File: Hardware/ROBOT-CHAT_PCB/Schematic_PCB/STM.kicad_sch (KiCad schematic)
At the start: 30 parts, among them J1 Conn_01x04, J2 Conn_02x07_Odd_Even, J3 Conn_01x02, J4 Conn_01x02, SW1 SW_Push_Dual, U1 STM32WB55CEUx, Y1 32.768kHz, Y2 32MHz

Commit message: current schematic
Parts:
- removed J2: Conn_02x07_Odd_Even, symbol Connector_Generic:Conn_02x07_Odd_Even
- added J201: Conn_ST_STDC14, Connector_PinHeader_1.27mm:PinHeader_2x07_P1.27mm_Vertical_SMD, symbol Connector:Conn_ST_STDC14
- C10, C11, C12, C13, C15, C16, C3, C4, C5, C6, C7, C8, C9: footprint (none) -> Capacitor_SMD:C_0603_1608Metric
- C14, C17, C18: footprint (none) -> Capacitor_SMD:C_0402_1005Metric
- D1: footprint (none) -> LED_SMD:LED_0603_1608Metric
- J1: footprint (none) -> Connector_JST:JST_XH_B4B-XH-AM_1x04_P2.50mm_Vertical
- J3, J4: footprint (none) -> Connector_JST:JST_PH_B2B-PH-K_1x02_P2.00mm_Vertical
- L1, L2: footprint (none) -> Inductor_SMD:L_0603_1608Metric
- R4, R5, R6: footprint (none) -> Resistor_SMD:R_0603_1608Metric
- SW1: footprint Button_Switch_SMD2:SW_Push_1P1T_NO_6x6mm_H9.5mm -> SW_Push_1P1T_NO_6x6mm_H9.5mm:SW_Push_1P1T_NO_6x6mm_H9.5mm
- Y2: footprint ABS07AIG_32_768KHZ_7_T:XTAL320X150X90 -> XRCGB32M000F2P01R0:XRCGB32M000F2P01R0
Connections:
- net +3.3V: now also J201.3 (VCC)
- net GND: now also J201.11 (GNDDetect), J201.5 (GND), J201.7 (GND)
- net NRST: now also J201.12 (~{RST})
- net SWCLK: now also J201.6 (JCLK/SWCLK)
- net SWDIO: now also J201.4 (JTMS/SWDIO)
- net SWO: now also J201.8 (JTDO/SWO)
- net VCP_RX: now also J201.13 (VCP_RX)
- net VCP_TX: now also J201.14 (VCP_TX)
- net EN3.3: no longer names the net of U1.19 (PB2)
- net EN5: no longer names the net of U1.45 (PB5)

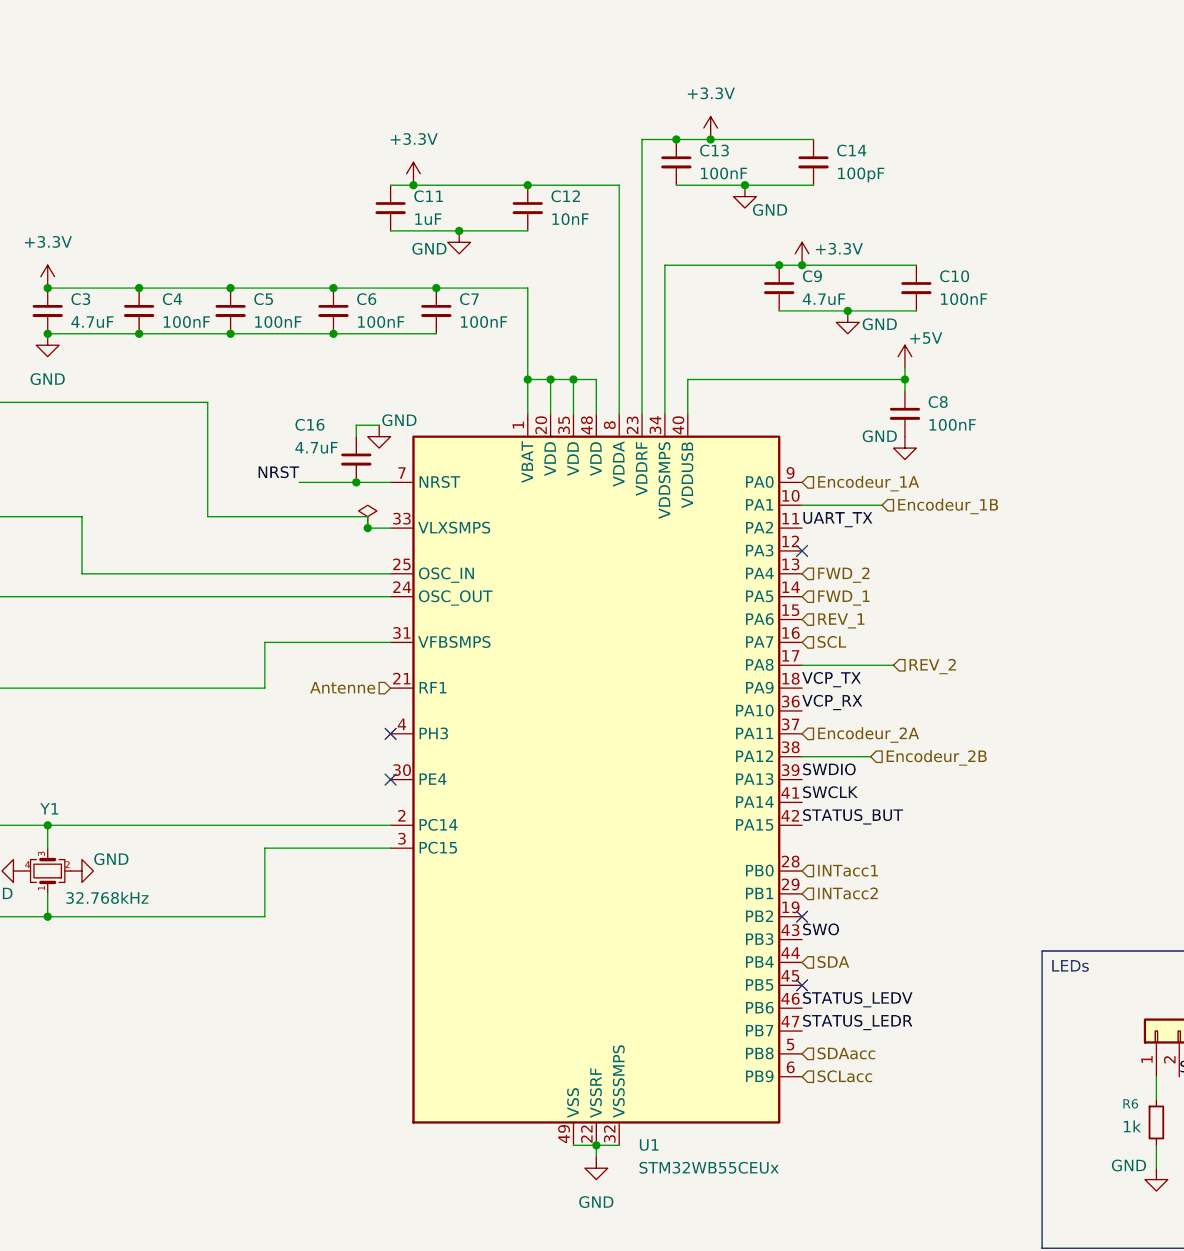
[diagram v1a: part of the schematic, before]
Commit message: Rerouting avec Mr Fiack
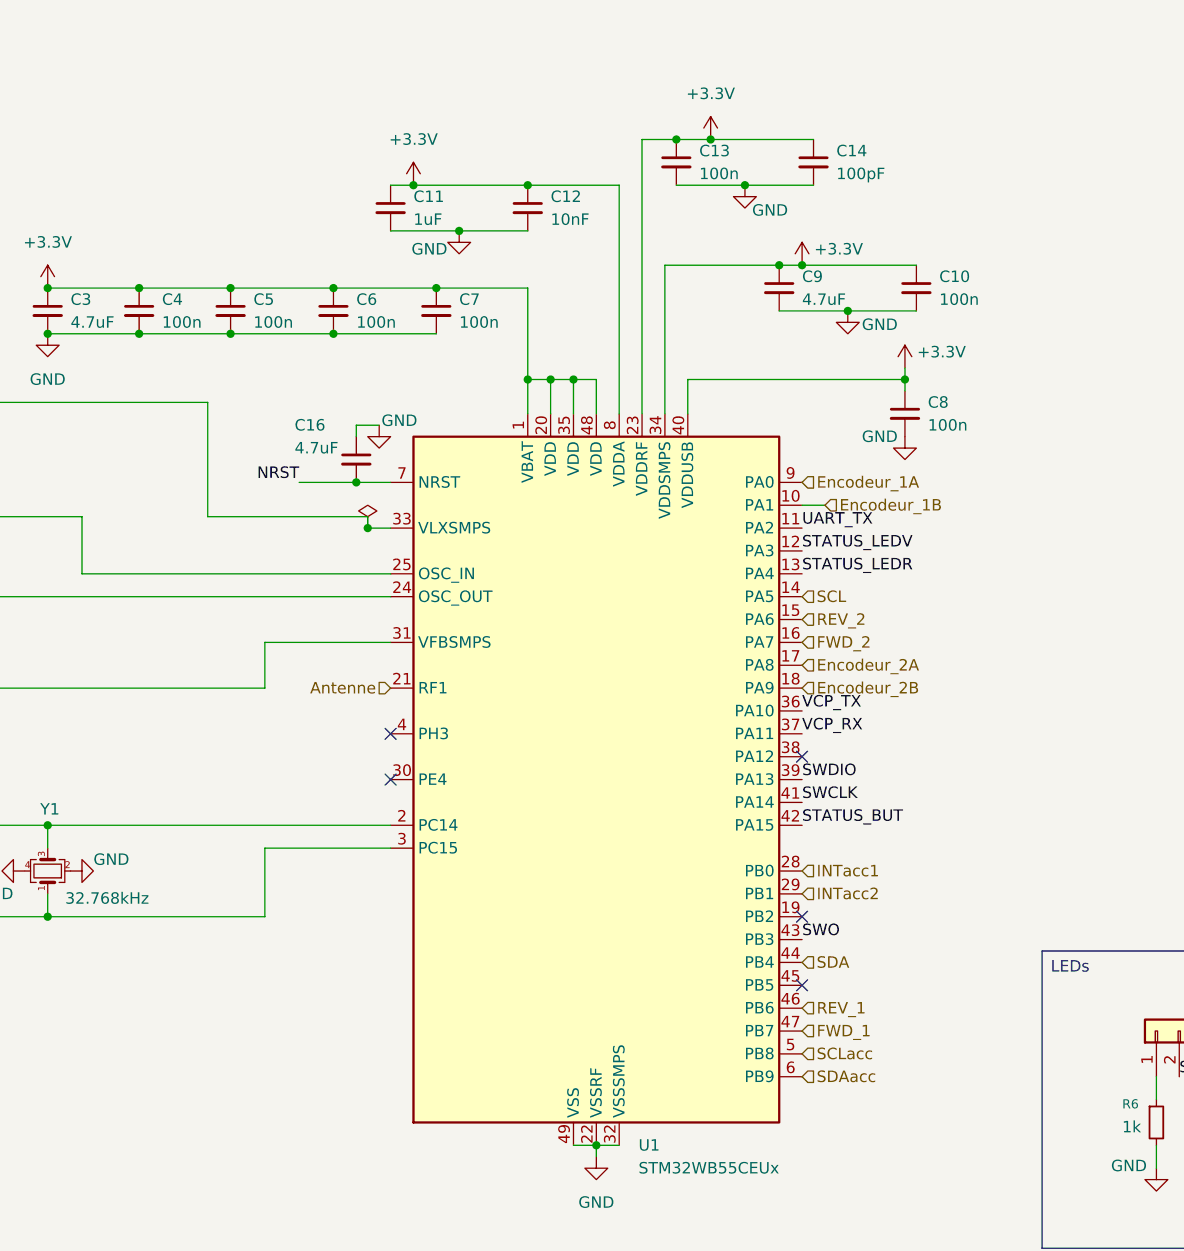
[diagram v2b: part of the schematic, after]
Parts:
- C10, C13, C4, C5, C6, C7, C8: value 100nF -> 100n; footprint Capacitor_SMD:C_0603_1608Metric -> Capacitor_SMD:C_0402_1005Metric
- C12: footprint Capacitor_SMD:C_0603_1608Metric -> Capacitor_SMD:C_0402_1005Metric
- R4, R5, R6: footprint Resistor_SMD:R_0603_1608Metric -> Resistor_SMD:R_0402_1005Metric
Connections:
- net +3.3V: now also C8.1, U1.40 (VDDUSB)
- net +5V: no longer C8.1, U1.40 (VDDUSB)
- net Encodeur_2A: now also U1.17 (PA8); no longer U1.37 (PA11)
- net Encodeur_2B: now also U1.18 (PA9); no longer U1.38 (PA12)
- net FWD_1: now also U1.47 (PB7); no longer U1.14 (PA5)
- net FWD_2: now also U1.16 (PA7); no longer U1.13 (PA4)
- net REV_1: now also U1.46 (PB6); no longer U1.15 (PA6)
- net REV_2: now also U1.15 (PA6); no longer U1.17 (PA8)
- net SCL: now also U1.14 (PA5); no longer U1.16 (PA7)
- net SCLacc: now also U1.5 (PB8); no longer U1.6 (PB9)
- net SDAacc: now also U1.6 (PB9); no longer U1.5 (PB8)
- net STATUS_LEDR: now also U1.13 (PA4); no longer U1.47 (PB7)
- net STATUS_LEDV: now also U1.12 (PA3); no longer U1.46 (PB6)
- net VCP_RX: now also U1.37 (PA11); no longer U1.36 (PA10)
- net VCP_TX: now also U1.36 (PA10); no longer U1.18 (PA9)
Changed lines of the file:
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@@
 	)
 	(no_connect
-		(at 177.8 82.55)
+		(at 177.8 105.41)
 	)
 	(no_connect
@@
 	(wire
 		(pts
-			(xy 185.42 105.41) (xy 177.8 105.41)
-		)
-		(stroke
-			(width 0)
-			(type default)
-		)
-	)
-	(wire
-		(pts
 			(xy 189.23 63.5) (xy 189.23 64.77)
 		)
@@
 	(wire
 		(pts
-			(xy 186.69 77.47) (xy 177.8 77.47)
-		)
-		(stroke
-			(width 0)
-			(type default)
-		)
-	)
-	(wire
-		(pts
-			(xy 187.96 95.25) (xy 177.8 95.25)
+			(xy 180.34 77.47) (xy 177.8 77.47)
 		)
 		(stroke
@@
 	)
 	(label "VCP_RX"
-		(at 177.8 100.33 0)
+		(at 177.8 102.87 0)
 		(effects
 			(font
@@
 	)
 	(label "VCP_TX"
-		(at 177.8 97.79 0)
+		(at 177.8 100.33 0)
 		(effects
 			(font
@@
 	)
 	(label "STATUS_LEDR"
-		(at 177.8 135.89 0)
+		(at 177.8 85.09 0)
 		(effects
 			(font
@@
 	)
 	(label "STATUS_LEDV"
-		(at 177.8 133.35 0)
+		(at 177.8 82.55 0)
 		(effects
 			(font
@@
 	(hierarchical_label "FWD_2"
 		(shape input)
-		(at 177.8 85.09 0)
+		(at 177.8 92.71 0)
 		(effects
 			(font
@@
 	(hierarchical_label "REV_1"
 		(shape input)
-		(at 177.8 90.17 0)
+		(at 177.8 133.35 0)
 		(effects
 			(font
@@
 	(hierarchical_label "Encodeur_2B"
 		(shape input)
-		(at 185.42 105.41 0)
+		(at 177.8 97.79 0)
 		(effects
 			(font
@@
 	(hierarchical_label "FWD_1"
 		(shape input)
-		(at 177.8 87.63 0)
+		(at 177.8 135.89 0)
 		(effects
 			(font
@@
 	(hierarchical_label "SDAacc"
 		(shape input)
-		(at 177.8 138.43 0)
+		(at 177.8 140.97 0)
 		(effects
 			(font
@@
 	(hierarchical_label "Encodeur_2A"
 		(shape input)
-		(at 177.8 102.87 0)
+		(at 177.8 95.25 0)
 		(effects
 			(font
@@
 	(hierarchical_label "SCLacc"
 		(shape input)
-		(at 177.8 140.97 0)
+		(at 177.8 138.43 0)
 		(effects
 			(font
@@
 	(hierarchical_label "REV_2"
 		(shape input)
-		(at 187.96 95.25 0)
+		(at 177.8 90.17 0)
 		(effects
 			(font
@@
 	(hierarchical_label "Encodeur_1B"
 		(shape input)
-		(at 186.69 77.47 0)
+		(at 180.34 77.47 0)
 		(effects
 			(font
@@
 	(hierarchical_label "SCL"
 		(shape input)
-		(at 177.8 92.71 0)
+		(at 177.8 87.63 0)
 		(effects
 			(font
@@
 			)
 		)
-		(property "Value" "100nF"
+		(property "Value" "100n"
 			(at 191.77 68.5862 0)
 			(effects
@@
 			)
 		)
-		(property "Footprint" "Capacitor_SMD:C_0603_1608Metric"
+		(property "Footprint" "Capacitor_SMD:C_0402_1005Metric"
 			(at 189.23 67.31 0)
 			(effects
@@
 			)
 		)
-		(property "Footprint" "Resistor_SMD:R_0603_1608Metric"
+		(property "Footprint" "Resistor_SMD:R_0402_1005Metric"
 			(at 217.17 146.05 0)
 			(effects
@@
 			)
 		)
-		(property "Footprint" "Capacitor_SMD:C_0603_1608Metric"
+		(property "Footprint" "Capacitor_SMD:C_0402_1005Metric"
 			(at 147.32 44.45 0)
 			(effects
@@
 			)
 		)
-		(property "Value" "100nF"
+		(property "Value" "100n"
 			(at 139.7 57.1562 0)
 			(effects
@@
 			)
 		)
-		(property "Footprint" "Capacitor_SMD:C_0603_1608Metric"
+		(property "Footprint" "Capacitor_SMD:C_0402_1005Metric"
 			(at 137.16 55.88 0)
 			(effects
@@
 			)
 		)
-		(property "Footprint" "Resistor_SMD:R_0603_1608Metric"
+		(property "Footprint" "Resistor_SMD:R_0402_1005Metric"
 			(at 242.57 146.05 0)
 			(effects
@@
 	)
 	(symbol
+		(lib_id "power:+3.3V")
+		(at 189.23 62.23 0)
+		(unit 1)
+		(exclude_from_sim no)
+		(in_bom yes)
+		(on_board yes)
+		(dnp no)
+		(property "Reference" "#PWR0201"
+			(at 189.23 66.04 0)
+			(effects
+				(font
+					(size 1.27 1.27)
+				)
+				(hide yes)
+			)
+		)
+		(property "Value" "+3.3V"
+			(at 193.294 60.452 0)
+			(effects
+				(font
+					(size 1.27 1.27)
+				)
+			)
+		)
+		(property "Footprint" ""
+			(at 189.23 62.23 0)
+			(effects
+				(font
+					(size 1.27 1.27)
+				)
+				(hide yes)
+			)
+		)
+		(property "Datasheet" ""
+			(at 189.23 62.23 0)
+			(effects
+				(font
+					(size 1.27 1.27)
+				)
+				(hide yes)
+			)
+		)
+		(property "Description" "Power symbol creates a global label with name \"+3.3V\""
+			(at 189.23 62.23 0)
+			(effects
+				(font
+					(size 1.27 1.27)
+				)
+				(hide yes)
+			)
+		)
+		(pin "1"
+		)
+		(instances
+			(project "PCB_robot_chat"
+				(path "/3534a4da-1897-4a3c-809d-843e7f41fadb/6dd21f76-e181-4380-95ef-cbdd4cbc38f9"
+					(reference "#PWR0201")
+					(unit 1)
+				)
+			)
+		)
+	)
+	(symbol
 		(lib_id "Device:C_Small")
 		(at 163.83 39.37 0)
@@
 			)
 		)
-		(property "Value" "100nF"
+		(property "Value" "100n"
 			(at 166.37 40.6462 0)
 			(effects
@@
 			)
 		)
-		(property "Footprint" "Capacitor_SMD:C_0603_1608Metric"
+		(property "Footprint" "Capacitor_SMD:C_0402_1005Metric"
 			(at 163.83 39.37 0)
 			(effects
@@
 			)
 		)
-		(property "Value" "100nF"
+		(property "Value" "100n"
 			(at 106.68 57.1562 0)
 			(effects
@@
 			)
 		)
-		(property "Footprint" "Capacitor_SMD:C_0603_1608Metric"
+		(property "Footprint" "Capacitor_SMD:C_0402_1005Metric"
 			(at 104.14 55.88 0)
 			(effects
@@
 			)
 		)
-		(property "Value" "100nF"
+		(property "Value" "100n"
 			(at 128.27 57.1562 0)
 			(effects
@@
 			)
 		)
-		(property "Footprint" "Capacitor_SMD:C_0603_1608Metric"
+		(property "Footprint" "Capacitor_SMD:C_0402_1005Metric"
 			(at 125.73 55.88 0)
 			(effects
@@
 			)
 		)
-		(property "Value" "100nF"
+		(property "Value" "100n"
 			(at 116.84 57.1562 0)
 			(effects
@@
 			)
 		)
-		(property "Footprint" "Capacitor_SMD:C_0603_1608Metric"
+		(property "Footprint" "Capacitor_SMD:C_0402_1005Metric"
 			(at 114.3 55.88 0)
 			(effects
@@
 	)
 	(symbol
-		(lib_id "power:+5V")
-		(at 189.23 62.23 0)
-		(unit 1)
-		(exclude_from_sim no)
-		(in_bom yes)
-		(on_board yes)
-		(dnp no)
-		(property "Reference" "#PWR015"
-			(at 189.23 66.04 0)
-			(effects
-				(font
-					(size 1.27 1.27)
-				)
-				(hide yes)
-			)
-		)
-		(property "Value" "+5V"
-			(at 191.516 58.928 0)
-			(effects
-				(font
-					(size 1.27 1.27)
-				)
-			)
-		)
-		(property "Footprint" ""
-			(at 189.23 62.23 0)
-			(effects
-				(font
-					(size 1.27 1.27)
-				)
-				(hide yes)
-			)
-		)
-		(property "Datasheet" ""
-			(at 189.23 62.23 0)
-			(effects
-				(font
-					(size 1.27 1.27)
-				)
-				(hide yes)
-			)
-		)
-		(property "Description" "Power symbol creates a global label with name \"+5V\""
-			(at 189.23 62.23 0)
-			(effects
-				(font
-					(size 1.27 1.27)
-				)
-				(hide yes)
-			)
-		)
-		(pin "1"
-		)
-		(instances
-			(project "PCB_robot_chat"
-				(path "/3534a4da-1897-4a3c-809d-843e7f41fadb/6dd21f76-e181-4380-95ef-cbdd4cbc38f9"
-					(reference "#PWR015")
-					(unit 1)
-				)
-			)
-		)
-	)
-	(symbol
 		(lib_id "Device:C_Small")
 		(at 190.5 53.34 0)
@@
 			)
 		)
-		(property "Value" "100nF"
+		(property "Value" "100n"
 			(at 193.04 54.6162 0)
 			(effects
@@
 			)
 		)
-		(property "Footprint" "Capacitor_SMD:C_0603_1608Metric"
+		(property "Footprint" "Capacitor_SMD:C_0402_1005Metric"
 			(at 190.5 53.34 0)
 			(effects
@@
 			)
 		)
-		(property "Footprint" "Resistor_SMD:R_0603_1608Metric"
+		(property "Footprint" "Resistor_SMD:R_0402_1005Metric"
 			(at 265.43 148.59 0)
 			(effects

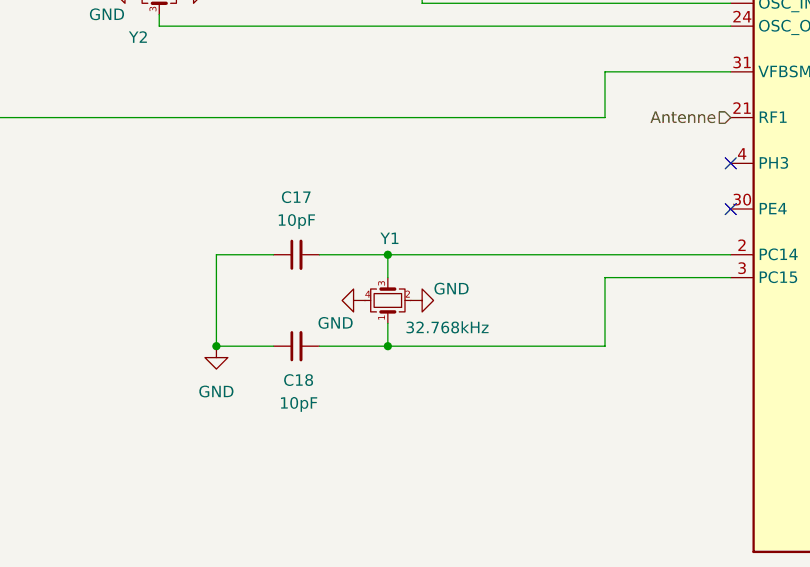
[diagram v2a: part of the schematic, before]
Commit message: Routage terminée, début serigraphie
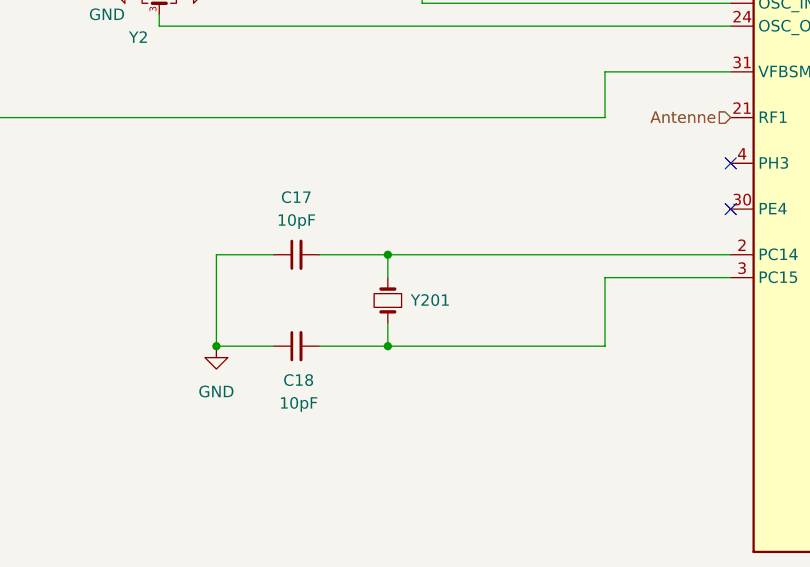
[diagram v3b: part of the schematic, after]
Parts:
- removed Y1: 32.768kHz, XRCGB32M000F2P01R0:XRCGB32M000F2P01R0, symbol Device:Crystal_GND24_Small
- added Y201: Crystal_Small, ABS07AIG-32.768KHZ-6-D-T:ABS07AIG-32.768KHZ-6-D-T, symbol Device:Crystal_Small
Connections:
- net at C18.2, U1.3 (PC15): now also Y201.1
- net at C17.2, U1.2 (PC14): now also Y201.2
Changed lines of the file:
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@@
+	)
+	(symbol
+		(lib_id "Device:Crystal_Small")
+		(at 93.98 118.11 90)
+		(unit 1)
+		(exclude_from_sim no)
+		(in_bom yes)
+		(on_board yes)
+		(dnp no)
+		(fields_autoplaced yes)
+		(property "Reference" "Y201"
+			(at 96.52 118.1099 90)
+			(effects
+				(font
+					(size 1.27 1.27)
+				)
+				(justify right)
+			)
+		)
+		(property "Value" "Crystal_Small"
+			(at 96.52 119.3799 90)
+			(effects
+				(font
+					(size 1.27 1.27)
+				)
+				(justify right)
+				(hide yes)
+			)
+		)
+		(property "Footprint" "ABS07AIG-32.768KHZ-6-D-T:ABS07AIG-32.768KHZ-6-D-T"
+			(at 93.98 118.11 0)
+			(effects
+				(font
+					(size 1.27 1.27)
+				)
+				(hide yes)
+			)
+		)
+		(property "Datasheet" "~"
+			(at 93.98 118.11 0)
+			(effects
+				(font
+					(size 1.27 1.27)
+				)
+				(hide yes)
+			)
+		)
+		(property "Description" "Two pin crystal, small symbol"
+			(at 93.98 118.11 0)
+			(effects
+				(font
+					(size 1.27 1.27)
+				)
+				(hide yes)
+			)
+		)
+		(pin "2"
+		)
+		(pin "1"
+		)
+		(instances
+			(project ""
+				(path "/3534a4da-1897-4a3c-809d-843e7f41fadb/6dd21f76-e181-4380-95ef-cbdd4cbc38f9"
+					(reference "Y201")
+					(unit 1)
+				)
+			)
+		)
 	)
 	(symbol
@@
 	)
 	(symbol
-		(lib_id "Device:Crystal_GND24_Small")
-		(at 93.98 118.11 90)
-		(unit 1)
-		(exclude_from_sim no)
-		(in_bom yes)
-		(on_board yes)
-		(dnp no)
-		(property "Reference" "Y1"
-			(at 94.234 111.252 90)
-			(effects
-				(font
-					(size 1.27 1.27)
-				)
-			)
-		)
-		(property "Value" "32.768kHz"
-			(at 100.584 121.158 90)
-			(effects
-				(font
-					(size 1.27 1.27)
-				)
-			)
-		)
-		(property "Footprint" "XRCGB32M000F2P01R0:XRCGB32M000F2P01R0"
-			(at 93.98 118.11 0)
-			(effects
-				(font
-					(size 1.27 1.27)
-				)
-				(hide yes)
-			)
-		)
-		(property "Datasheet" "~"
-			(at 93.98 118.11 0)
-			(effects
-				(font
-					(size 1.27 1.27)
-				)
-				(hide yes)
-			)
-		)
-		(property "Description" "Four pin crystal, GND on pins 2 and 4, small symbol"
-			(at 93.98 118.11 0)
-			(effects
-				(font
-					(size 1.27 1.27)
-				)
-				(hide yes)
-			)
-		)
-		(pin "1"
-		)
-		(pin "2"
-		)
-		(pin "4"
-		)
-		(pin "3"
-		)
-		(instances
-			(project "PCB_robot_chat"
-				(path "/3534a4da-1897-4a3c-809d-843e7f41fadb/6dd21f76-e181-4380-95ef-cbdd4cbc38f9"
-					(reference "Y1")
-					(unit 1)
-				)
-			)
-		)
-	)
-	(symbol
 		(lib_id "power:GND")
 		(at 189.23 69.85 0)
@@
 	(symbol
 		(lib_id "power:GND")
-		(at 96.52 118.11 90)
-		(unit 1)
-		(exclude_from_sim no)
-		(in_bom yes)
-		(on_board yes)
-		(dnp no)
-		(property "Reference" "#PWR021"
-			(at 102.87 118.11 0)
-			(effects
-				(font
-					(size 1.27 1.27)
-				)
-				(hide yes)
-			)
-		)
-		(property "Value" "GND"
-			(at 99.06 116.84 90)
-			(effects
-				(font
-					(size 1.27 1.27)
-				)
-				(justify right)
-			)
-		)
-		(property "Footprint" ""
-			(at 96.52 118.11 0)
-			(effects
-				(font
-					(size 1.27 1.27)
-				)
-				(hide yes)
-			)
-		)
-		(property "Datasheet" ""
-			(at 96.52 118.11 0)
-			(effects
-				(font
-					(size 1.27 1.27)
-				)
-				(hide yes)
-			)
-		)
-		(property "Description" "Power symbol creates a global label with name \"GND\" , ground"
-			(at 96.52 118.11 0)
-			(effects
-				(font
-					(size 1.27 1.27)
-				)
-				(hide yes)
-			)
-		)
-		(pin "1"
-		)
-		(instances
-			(project "PCB_robot_chat"
-				(path "/3534a4da-1897-4a3c-809d-843e7f41fadb/6dd21f76-e181-4380-95ef-cbdd4cbc38f9"
-					(reference "#PWR021")
-					(unit 1)
-				)
-			)
-		)
-	)
-	(symbol
-		(lib_id "power:GND")
 		(at 265.43 153.67 0)
 		(unit 1)
@@
 					(unit 1)
 				)
-			)
-		)
-	)
-	(symbol
-		(lib_id "power:GND")
-		(at 91.44 118.11 270)
-		(unit 1)
-		(exclude_from_sim no)
-		(in_bom yes)
-		(on_board yes)
-		(dnp no)
-		(property "Reference" "#PWR022"
-			(at 85.09 118.11 0)
-			(effects
-				(font
-					(size 1.27 1.27)
-				)
-				(hide yes)
-			)
-		)
-		(property "Value" "GND"
-			(at 90.17 120.65 90)
-			(effects
-				(font
-					(size 1.27 1.27)
-				)
-				(justify right)
-			)
-		)
-		(property "Footprint" ""
-			(at 91.44 118.11 0)
-			(effects
-				(font
-					(size 1.27 1.27)
-				)
-				(hide yes)
-			)
-		)
-		(property "Datasheet" ""
-			(at 91.44 118.11 0)
-			(effects
-				(font
-					(size 1.27 1.27)
-				)
-				(hide yes)
-			)
-		)
-		(property "Description" "Power symbol creates a global label with name \"GND\" , ground"
-			(at 91.44 118.11 0)
-			(effects
-				(font
-					(size 1.27 1.27)
-				)
-				(hide yes)
-			)
-		)
-		(pin "1"
-		)
-		(instances
-			(project "PCB_robot_chat"
-				(path "/3534a4da-1897-4a3c-809d-843e7f41fadb/6dd21f76-e181-4380-95ef-cbdd4cbc38f9"
-					(reference "#PWR022")
-					(unit 1)
-				)
